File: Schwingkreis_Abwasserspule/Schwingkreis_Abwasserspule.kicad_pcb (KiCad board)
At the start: 2 copper layers, 18 parts, among them J1 Power_Supply, J2 Coil_Connection, Q1 BC546, Q2 BC546, Q3 BC546, U1 TL082

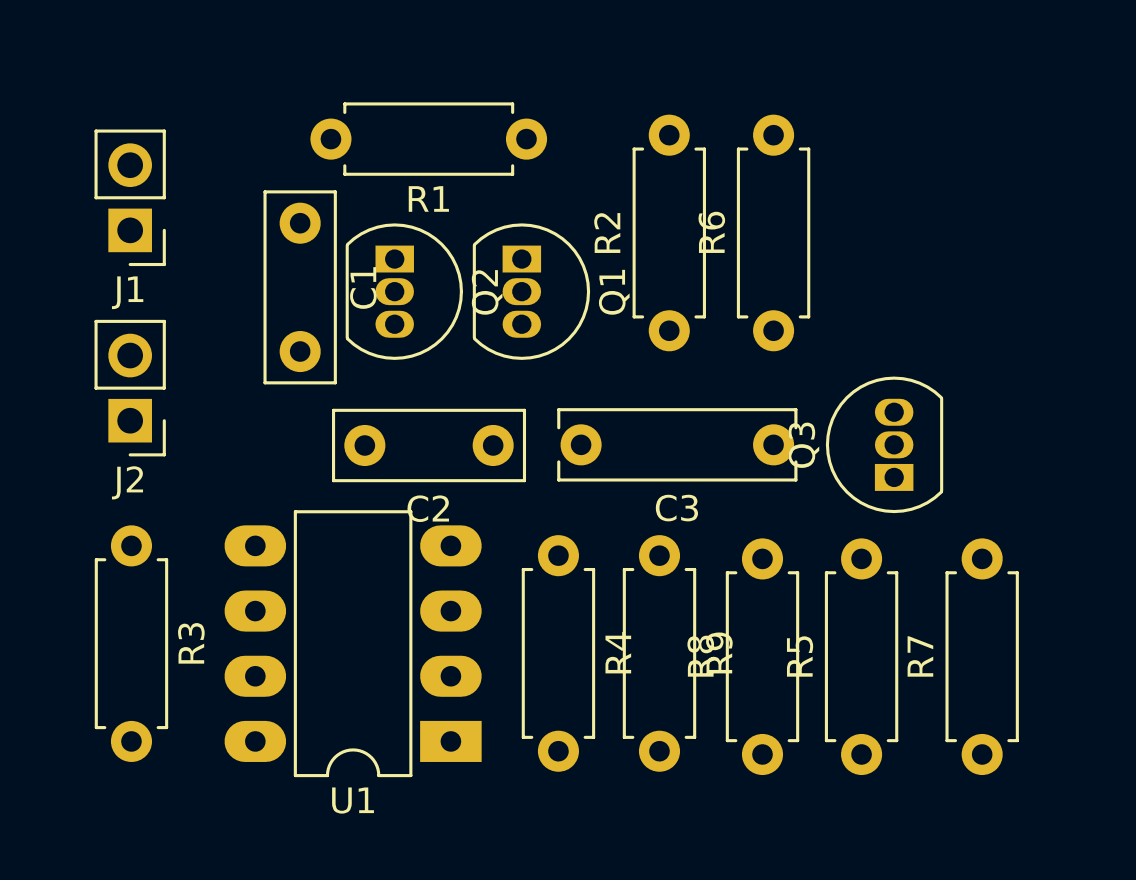
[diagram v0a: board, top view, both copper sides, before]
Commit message: final design for this version. ordered 5 times at jlcpcb
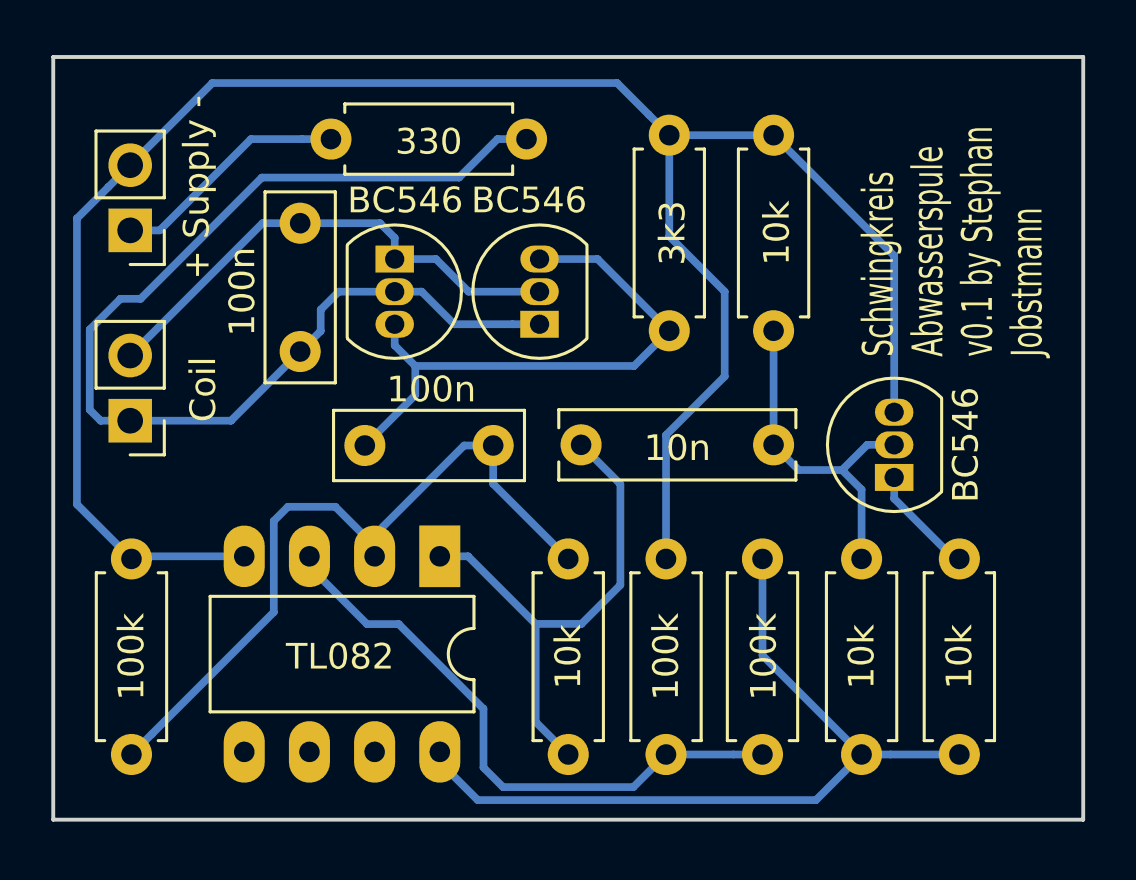
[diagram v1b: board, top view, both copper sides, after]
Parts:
- J1: value Power_Supply -> + Supply -
- J2: value Coil_Connection -> Coil
- moved U1 7.23 mm to (134.2, 111.7), turned to 270 degrees
- moved Q1 2.63 mm to (138.1, 102.6), turned to 90 degrees
- moved R7 0.89 mm to (154.4, 119.4)
- moved R3 0.51 mm to (122.2, 111.8)
- moved R4 0.40 mm to (139.2, 111.8)
- moved R9 0.28 mm to (143.0, 111.8)
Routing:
- net GND: track 0.00 -> 79.8 mm
- net Net-(C1-Pad2): track 0.00 -> 44.0 mm
- net +VDC: track 0.00 -> 31.2 mm
- net Net-(C2-Pad1): track 0.00 -> 29.1 mm
- net VCOM: track 0.00 -> 23.5 mm
- net Net-(C2-Pad2): track 0.00 -> 22.5 mm
- net Net-(C3-Pad2): track 0.00 -> 20.5 mm
- net Net-(C1-Pad1): track 0.00 -> 19.7 mm
- net Net-(C3-Pad1): track 0.00 -> 13.7 mm
- net Net-(J1-Pad1): track 0.00 -> 9.30 mm
- net Net-(Q3-Pad1): track 0.00 -> 4.34 mm
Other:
- board outline added: 40.1 x 29.7 mm
- net class POWER added: clearance 0.2, trace_width 0.3, via_dia 1, via_drill 0.6
- net class SIGNAL added: clearance 0.2, trace_width 0.3, via_dia 1, via_drill 0.6
- board text added: "Schwingkreis Abwasserspule v0.1 by Stephan Jobstmann"
